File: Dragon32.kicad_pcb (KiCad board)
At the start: 2 copper layers, 253 x 169.1 mm, 139 parts, among them IC10 74ACT138, IC11 74ACT244N, IC16 74ACT244N, IC18 74ACT08, IC19 MC6809E, IC20 MC14529B, IC24 74ACT244N, IC25 LM393P, IC31 74ACT02, IC33 74AACT138N, IC34 CD4050BDR, J1 Video Output Female, J2 Board Interconnect Female, J3 Conn_02x08_Odd_Even, J4 JTAG, J5 6-bit DAC, SW1 RESET, U1 AS6C1008-TIN, U2 AS6C1008-55TIN, U3 XC95144XL-TQ100, U4 TPS7A2433DBVR, U5 W65C21, U6 W65C21, U7 W65C21, U8 28C256, X1 14.31818MHz

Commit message: serial wiring
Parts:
- removed IC18: 74ACT08, Package_SO:SOIC-14_3.9x8.7mm_P1.27mm
- removed IC20: MC14529B, Package_DIP:DIP-16_W7.62mm
- removed IC25: LM393P, Package_DIP:DIP-8_W7.62mm
- added C10: 100n, Capacitor_SMD:C_0805_2012Metric_Pad1.18x1.45mm_HandSolder, F.Cu at (154.9, 79.4)
- added C17: 100n, Capacitor_SMD:C_0805_2012Metric_Pad1.18x1.45mm_HandSolder, F.Cu at (121.1, 77.0)
- added C18: 1u, Capacitor_Tantalum_SMD:CP_EIA-3216-18_Kemet-A_Pad1.58x1.35mm_HandSolder, F.Cu at (137.0, 37.0)
- added C19: 1u, Capacitor_Tantalum_SMD:CP_EIA-3216-18_Kemet-A_Pad1.58x1.35mm_HandSolder, F.Cu at (145.2, 37.0)
- added D10: 1N914, Diode_SMD:D_SOD-323_HandSoldering, F.Cu at (133.3, 74.4)
- added D11: 1N914, Diode_SMD:D_SOD-323_HandSoldering, B.Cu at (133.3, 74.4)
- added D12: 1N914, Diode_SMD:D_SOD-323_HandSoldering, F.Cu at (121.2, 74.4)
- added D13: 1N914, Diode_SMD:D_SOD-323_HandSoldering, B.Cu at (121.2, 74.4)
- added D14: 1N914, Diode_SMD:D_SOD-323_HandSoldering, B.Cu at (123.4, 59.5)
- added D15: 1N914, Diode_SMD:D_SOD-323_HandSoldering, F.Cu at (123.4, 59.5)
- added D16: 1N914, Diode_SMD:D_SOD-323_HandSoldering, F.Cu at (128.4, 59.5)
- added D17: 1N914, Diode_SMD:D_SOD-323_HandSoldering, B.Cu at (128.4, 59.5)
- added IC1: LM393DR, Package_SO:SOP-8_3.9x4.9mm_P1.27mm, F.Cu at (147.2, 151.1)
- added JP3: Serial, Jumper:SolderJumper-3_P1.3mm_Open_Pad1.0x1.5mm, F.Cu at (143.1, 70.2)
- added PL9: Serial, Dragon:DIN-7_DELTRON_671-0701_Horizontal, F.Cu at (86.5, 135.2)
- added R28: 4K7, Resistor_SMD:R_0805_2012Metric_Pad1.20x1.40mm_HandSolder, B.Cu at (96.2, 81.9)
- added R33: 10M, Resistor_SMD:R_0805_2012Metric_Pad1.20x1.40mm_HandSolder, B.Cu at (147.3, 154.1)
- added R34: 1K, Resistor_SMD:R_0805_2012Metric_Pad1.20x1.40mm_HandSolder, B.Cu at (151.9, 147.4)
- added R35: 47R, Resistor_SMD:R_0805_2012Metric_Pad1.20x1.40mm_HandSolder, B.Cu at (92.7, 129.2)
- added R37: 47R, Resistor_SMD:R_0805_2012Metric_Pad1.20x1.40mm_HandSolder, B.Cu at (92.7, 132.5)
- added R44: 4K7, Resistor_SMD:R_0805_2012Metric_Pad1.20x1.40mm_HandSolder, B.Cu at (98.1, 118.2)
- added R57: 47K, Resistor_SMD:R_0805_2012Metric_Pad1.20x1.40mm_HandSolder, B.Cu at (132.8, 77.0)
- added R58: 47K, Resistor_SMD:R_0805_2012Metric_Pad1.20x1.40mm_HandSolder, B.Cu at (126.9, 76.0)
- added R59: 100K, Resistor_SMD:R_0805_2012Metric_Pad1.20x1.40mm_HandSolder, F.Cu at (120.3, 64.3)
- added R60: 100K, Resistor_SMD:R_0805_2012Metric_Pad1.20x1.40mm_HandSolder, F.Cu at (120.3, 62.3)
- added REG1: LM79L05_TO92, Package_TO_SOT_SMD:SOT-89-3_Handsoldering, F.Cu at (141.2, 38.0)
- added U10: 4052, Package_SO:TSSOP-16_4.4x5mm_P0.65mm, F.Cu at (148.5, 133.8)
- added U11: TS5A3166DBVR, Package_TO_SOT_SMD:SOT-23-5, F.Cu at (149.8, 141.1)
- added U12: ~, Package_DIP:DIP-28_W15.24mm, F.Cu at (137.1, 47.4)
- added U13: 4069, Package_SO:SOIC-14_3.9x8.7mm_P1.27mm, F.Cu at (127.1, 66.4)
- added U14: LM348DR, Package_SO:SOIC-14_3.9x8.7mm_P1.27mm, F.Cu at (127.1, 77.0)
- added U9: 74HCT1G08, Package_TO_SOT_SMD:SOT-353_SC-70-5_Handsoldering, B.Cu at (209.3, 116.2)
- added X2: 1.8432MHz, Crystal:Crystal_HC18-U_Horizontal_1EP_style2, F.Cu at (128.0, 54.1)
- C1, C30, C31, C32, C33, C4, C43, C44, D4, D5, D7, D8, D9, R11, R13, R15, R18, R19, R21, R24, R25, R27, R39, R45, R46, R47, R5, R50, R52, R6, R8: moved to F.Cu
- IC10: footprint Package_SO:SOIC-20W_7.5x12.8mm_P1.27mm -> Package_SO:SOIC-16W_7.5x10.3mm_P1.27mm
- IC33: value 74AACT138N -> 74ACT138N; footprint Package_SO:SOIC-20W_7.5x12.8mm_P1.27mm -> Package_SO:SOIC-16W_7.5x10.3mm_P1.27mm
- R31: value 4K7 -> 10K
- R53: value 10M -> 4K7
- R54: value 1K -> 4K7
- R55: value 10K -> 4K7
- TR1: value PN2222 -> PZT2222A; footprint Package_TO_SOT_THT:TO-92_Inline_Wide -> Package_TO_SOT_SMD:SOT-223-3_TabPin2
- moved R38 279.0 mm to (91.3, 175.6)
- moved R29 191.1 mm to (214.8, 156.6), turned to 180 degrees
- moved R16 186.8 mm to (214.8, 152.5)
- moved C26 185.3 mm to (214.8, 154.6)
- moved R56 169.9 mm to (197.0, 191.6), turned to 90 degrees
- moved C11 169.4 mm to (221.7, 46.0), turned to 90 degrees
- moved C12 162.0 mm to (226.7, 52.8), turned to -90 degrees
- moved R63 158.1 mm to (208.5, 182.6), turned to 180 degrees
- moved D6 157.4 mm to (109.3, 37.6), turned to 180 degrees
- moved D5 155.1 mm to (109.3, 41.6), turned to 0 degrees
- moved R36 154.9 mm to (109.3, 35.5)
- moved D4 154.6 mm to (109.4, 39.6), turned to 0 degrees
- moved C13 145.4 mm to (215.0, 53.3), turned to 0 degrees
- moved C48 142.7 mm to (211.5, 155.6), turned to -90 degrees
- moved C14 140.6 mm to (238.4, 64.2), turned to 0 degrees
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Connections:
- IC16 pad 11: DO7 -> DO3
- IC16 pad 12: D6 -> D4
- IC16 pad 13: DO1 -> DO2
- IC16 pad 14: D5 -> D0
- IC16 pad 15: DO0 -> DO5
- IC16 pad 16: D2 -> D1
- IC16 pad 17: DO4 -> DO6
- IC16 pad 18: D3 -> D7
- IC16 pad 2: DO3 -> DO7
- IC16 pad 3: D4 -> D6
- IC16 pad 4: DO2 -> DO1
- IC16 pad 5: D0 -> D5
- IC16 pad 6: DO5 -> DO0
- IC16 pad 7: D1 -> D2
- IC16 pad 8: DO6 -> DO4
- IC16 pad 9: D7 -> D3
- IC34 pad 10: DAC5 -> DAC2
- IC34 pad 11: PIADAC3 -> PIADAC1
- IC34 pad 12: DAC3 -> DAC1
- IC34 pad 2: DAC1 -> DAC5
- IC34 pad 3: PIADAC1 -> PIADAC5
- IC34 pad 4: DAC2 -> DAC4
- IC34 pad 5: PIADAC2 -> PIADAC4
- IC34 pad 6: DAC4 -> DAC3
- IC34 pad 7: PIADAC4 -> PIADAC3
- IC34 pad 9: PIADAC5 -> PIADAC2
- PL6 pad 1: +12V -> BIAS
- PL6 pad 3: -5V -> SOUND
- PL6 pad 4: GND -> VID OUT
- PL6 pad 6: VID OUT -> GND
- PL6 pad 7: SOUND -> -12V
- PL6 pad 9: BIAS -> +12V
- R2 pad 1: unconnected-(R2-Pad1) -> ~{RAS0}
- R31 pad 1: CASS -> Net-(IC1B-+)
- R31 pad 2: +5V -> Net-(U10-X)
- R53 pad 1: PA7 -> Net-(PL9-Pad7)
- R53 pad 2: Net-(IC25B-+) -> -12V
- R54 pad 1: +5V -> Net-(PL9-Pad5)
- R54 pad 2: PA7 -> Net-(D10-A)
- R55 pad 1: Net-(IC25B-+) -> Net-(PL9-Pad2)
- TR1 pad 1: GND -> Net-(TR1-B)
- TR1 pad 2: Net-(TR1-B) -> Net-(D1-A)
- TR1 pad 3: Net-(D1-A) -> GND
- U5 pad 24: +5V -> Net-(JP3-C)
- U5 pad 26: +5V -> Net-(JP3-C)
- U7 pad 11: Alpha -> RC
- U7 pad 12: Inverse -> RClk
- U7 pad 14: RClk -> Inverse
- U7 pad 15: RC -> Alpha
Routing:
- net +5V: track 0.00 -> 1586.9 mm, vias 0 -> 37
- net R/~{W}: track 0.00 -> 592.3 mm, vias 0 -> 15
- net D7: track 0.00 -> 539.6 mm, vias 0 -> 11
- net D6: track 0.00 -> 531.6 mm, vias 0 -> 10
- net D4: track 0.00 -> 529.8 mm, vias 0 -> 11
- net D1: track 0.00 -> 526.3 mm, vias 0 -> 11
- net D0: track 0.00 -> 520.6 mm, vias 0 -> 10
- net D5: track 0.00 -> 520.4 mm, vias 0 -> 10
- net A1: track 0.00 -> 518.5 mm, vias 0 -> 11
- net A0: track 0.00 -> 515.7 mm, vias 0 -> 11
- net ~{RES}: track 0.00 -> 512.4 mm, vias 0 -> 9
- net D2: track 0.00 -> 508.1 mm, vias 0 -> 11
- net D3: track 0.00 -> 508.0 mm, vias 0 -> 10
- net E: track 0.00 -> 490.2 mm, vias 0 -> 11
- net +12V: track 0.00 -> 450.8 mm, vias 0 -> 4
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- added copper zone on B.Cu, net +12V
- added copper zone on B.Cu, net +5V
- added copper zone on F.Cu, net +5V
- added copper zone on F.Cu, net -5V

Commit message: add audio circuits
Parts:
- added C20: 18pF, Capacitor_SMD:C_0805_2012Metric_Pad1.18x1.45mm_HandSolder, F.Cu at (174.6, 25.9)
- added C21: 100nF, Capacitor_SMD:C_0805_2012Metric_Pad1.18x1.45mm_HandSolder, F.Cu at (177.6, 25.9)
- added C24: 18pF, Capacitor_SMD:C_0805_2012Metric_Pad1.18x1.45mm_HandSolder, F.Cu at (180.6, 25.9)
- added C25: 18pF, Capacitor_SMD:C_0805_2012Metric_Pad1.18x1.45mm_HandSolder, F.Cu at (183.6, 25.9)
- added C28: 100nF, Capacitor_SMD:C_0805_2012Metric_Pad1.18x1.45mm_HandSolder, F.Cu at (186.6, 25.9)
- added C29: 18pF, Capacitor_SMD:C_0805_2012Metric_Pad1.18x1.45mm_HandSolder, F.Cu at (174.6, 21.1)
- added C34: 100nF, Capacitor_SMD:C_0805_2012Metric_Pad1.18x1.45mm_HandSolder, F.Cu at (177.6, 21.1)
- added C36: 100nF, Capacitor_SMD:C_0805_2012Metric_Pad1.18x1.45mm_HandSolder, F.Cu at (180.6, 21.1)
- added C37: 2.2nF, Capacitor_SMD:C_0805_2012Metric_Pad1.18x1.45mm_HandSolder, F.Cu at (183.6, 21.1)
- added C40: 2.2nF, Capacitor_SMD:C_0805_2012Metric_Pad1.18x1.45mm_HandSolder, F.Cu at (186.6, 21.1)
- added C41: 2.2nF, Capacitor_SMD:C_0805_2012Metric_Pad1.18x1.45mm_HandSolder, F.Cu at (174.6, 16.3)
- added C46: 10uF, Capacitor_SMD:CP_Elec_5x3, F.Cu at (178.6, 50.4)
- added C47: 2.2nF, Capacitor_SMD:C_0805_2012Metric_Pad1.18x1.45mm_HandSolder, F.Cu at (177.6, 16.3)
- added C49: 2.2nF, Capacitor_SMD:C_0805_2012Metric_Pad1.18x1.45mm_HandSolder, F.Cu at (180.6, 16.3)
- added C50: 2.2nF, Capacitor_SMD:C_0805_2012Metric_Pad1.18x1.45mm_HandSolder, F.Cu at (183.6, 16.3)
- added C51: 10uF, Capacitor_SMD:CP_Elec_5x3, F.Cu at (194.3, 50.3)
- added J6: UART, Connector_PinHeader_1.27mm:PinHeader_1x04_P1.27mm_Vertical, F.Cu at (162.5, 56.3)
- added J7: ICSP, Connector_PinHeader_1.27mm:PinHeader_2x03_P1.27mm_Vertical, F.Cu at (181.3, 56.6)
- added J8: UART, Connector_PinHeader_1.27mm:PinHeader_1x04_P1.27mm_Vertical, F.Cu at (187.3, 55.0)
- added J9: ICSP, Connector_PinHeader_1.27mm:PinHeader_2x03_P1.27mm_Vertical, F.Cu at (203.4, 60.0)
- added JP5: J1 CFG0, Jumper:SolderJumper-2_P1.3mm_Open_Pad1.0x1.5mm, F.Cu at (187.7, 37.3)
- added JP7: J2 CFG1, Jumper:SolderJumper-2_P1.3mm_Open_Pad1.0x1.5mm, F.Cu at (187.7, 40.9)
- added R61: 3.6K, Resistor_SMD:R_0805_2012Metric_Pad1.20x1.40mm_HandSolder, F.Cu at (189.6, 25.9)
- added R62: 3.6K, Resistor_SMD:R_0805_2012Metric_Pad1.20x1.40mm_HandSolder, F.Cu at (192.6, 25.9)
- added R64: 3.6K, Resistor_SMD:R_0805_2012Metric_Pad1.20x1.40mm_HandSolder, F.Cu at (195.5, 25.9)
- added R65: 1K, Resistor_SMD:R_0805_2012Metric_Pad1.20x1.40mm_HandSolder, F.Cu at (198.5, 25.9)
- added R66: 1K, Resistor_SMD:R_0805_2012Metric_Pad1.20x1.40mm_HandSolder, F.Cu at (201.4, 25.9)
- added R67: 1K, Resistor_SMD:R_0805_2012Metric_Pad1.20x1.40mm_HandSolder, F.Cu at (189.6, 21.2)
- added R68: 1K, Resistor_SMD:R_0805_2012Metric_Pad1.20x1.40mm_HandSolder, F.Cu at (192.6, 21.2)
- added R69: 3.6K, Resistor_SMD:R_0805_2012Metric_Pad1.20x1.40mm_HandSolder, F.Cu at (195.5, 21.2)
- added R70: 3.6K, Resistor_SMD:R_0805_2012Metric_Pad1.20x1.40mm_HandSolder, F.Cu at (198.5, 21.2)
- added R71: 3.6K, Resistor_SMD:R_0805_2012Metric_Pad1.20x1.40mm_HandSolder, F.Cu at (201.4, 21.2)
- added R72: 1K, Resistor_SMD:R_0805_2012Metric_Pad1.20x1.40mm_HandSolder, F.Cu at (189.6, 16.4)
- added R73: 1K, Resistor_SMD:R_0805_2012Metric_Pad1.20x1.40mm_HandSolder, F.Cu at (192.6, 16.4)
- added R74: 1K, Resistor_SMD:R_0805_2012Metric_Pad1.20x1.40mm_HandSolder, F.Cu at (195.5, 16.4)
- added R75: 1K, Resistor_SMD:R_0805_2012Metric_Pad1.20x1.40mm_HandSolder, F.Cu at (198.5, 16.4)
- added U15: ATmega48PA-A, Package_QFP:TQFP-32_7x7mm_P0.8mm, F.Cu at (174.0, 68.3)
- added U16: ATmega48PA-A, Package_QFP:TQFP-32_7x7mm_P0.8mm, F.Cu at (195.2, 68.3)
- added U17: 74LS08, Package_SO:SO-14_3.9x8.65mm_P1.27mm, F.Cu at (202.7, 51.9)
- added X3: 27MHz, Crystal:Crystal_SMD_3225-4Pin_3.2x2.5mm_HandSoldering, F.Cu at (171.0, 59.3)
- added X4: 27MHz, Crystal:Crystal_SMD_3225-4Pin_3.2x2.5mm_HandSoldering, F.Cu at (192.3, 59.2)
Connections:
- net SOUND renamed OUT_L
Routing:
- net OUT_L: track 213.2 -> 248.6 mm
- net VCLK: track 284.2 -> 298.1 mm, vias 5 -> 3
- net A2: track 420.2 -> 416.0 mm, vias 10 -> 9
- net GND: vias 120 -> 121

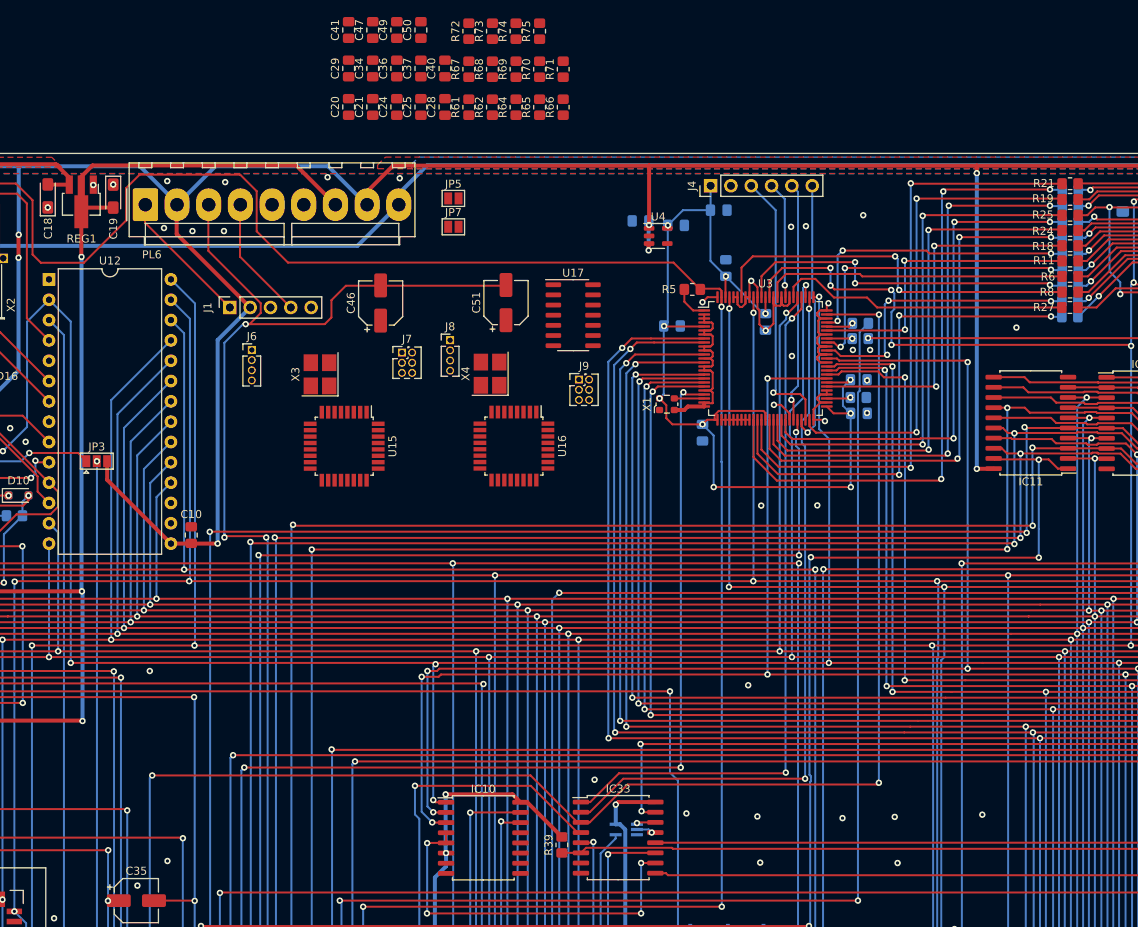
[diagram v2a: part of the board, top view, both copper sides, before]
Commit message: complete audio routing
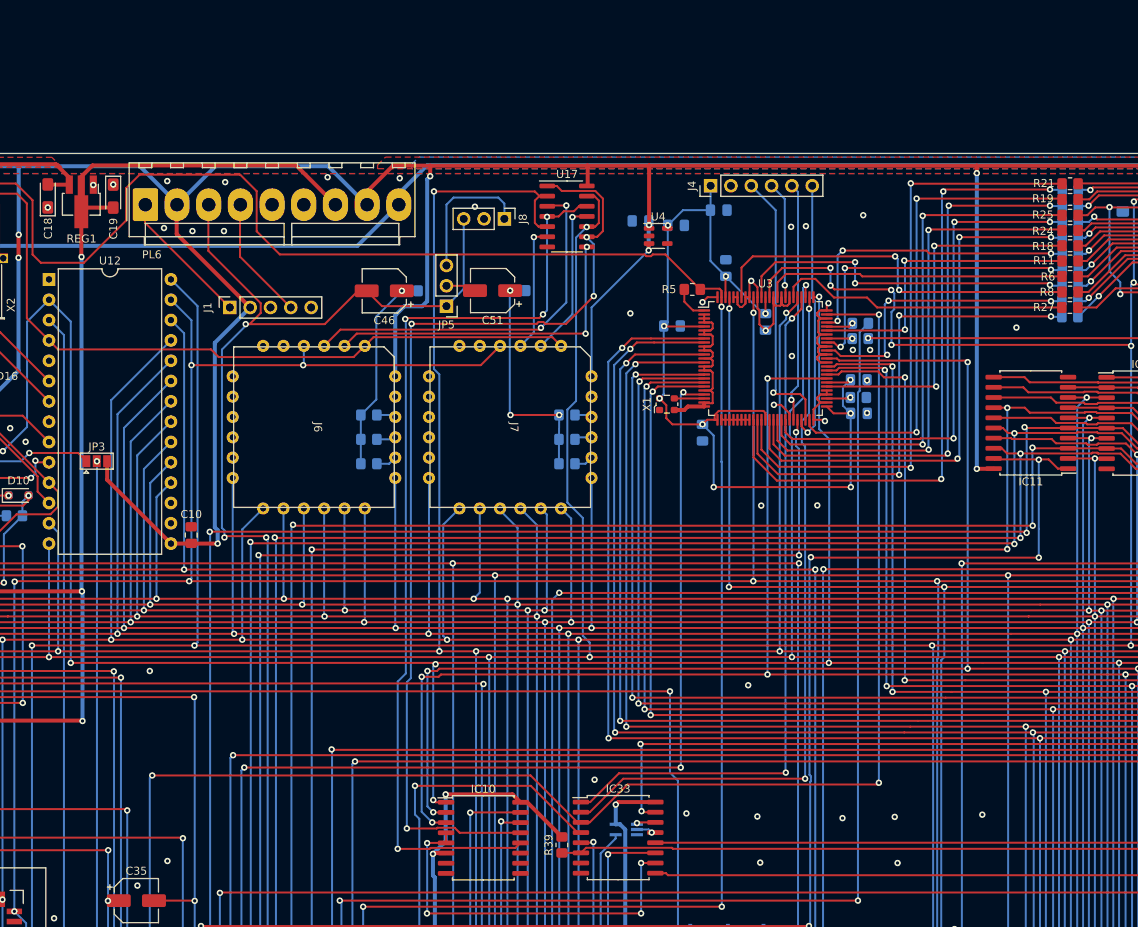
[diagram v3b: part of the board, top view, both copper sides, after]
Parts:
- removed C20, C24, C25, C29: 18pF, Capacitor_SMD:C_0805_2012Metric_Pad1.18x1.45mm_HandSolder
- removed C21, C28, C34, C36: 100nF, Capacitor_SMD:C_0805_2012Metric_Pad1.18x1.45mm_HandSolder
- removed C37, C40, C41, C47, C49, C50: 2.2nF, Capacitor_SMD:C_0805_2012Metric_Pad1.18x1.45mm_HandSolder
- removed J9: ICSP, Connector_PinHeader_1.27mm:PinHeader_2x03_P1.27mm_Vertical
- removed JP7: J2 CFG1, Jumper:SolderJumper-2_P1.3mm_Open_Pad1.0x1.5mm
- removed R61, R62, R64, R69, R70, R71: 3.6K, Resistor_SMD:R_0805_2012Metric_Pad1.20x1.40mm_HandSolder
- removed U15, U16: ATmega48PA-A, Package_QFP:TQFP-32_7x7mm_P0.8mm
- removed X3, X4: 27MHz, Crystal:Crystal_SMD_3225-4Pin_3.2x2.5mm_HandSoldering
- J6: value UART -> Audio Left; footprint Connector_PinHeader_1.27mm:PinHeader_1x04_P1.27mm_Vertical -> Dragon:AY-QTHT
- J7: value ICSP -> Audio Right; footprint Connector_PinHeader_1.27mm:PinHeader_2x03_P1.27mm_Vertical -> Dragon:AY-QTHT
- J8: value UART -> Stereo; footprint Connector_PinHeader_1.27mm:PinHeader_1x04_P1.27mm_Vertical -> Connector_PinHeader_2.54mm:PinHeader_1x03_P2.54mm_Vertical
- JP5: value J1 CFG0 -> Jumper_3_Open; footprint Jumper:SolderJumper-2_P1.3mm_Open_Pad1.0x1.5mm -> Connector_PinHeader_2.54mm:PinHeader_1x03_P2.54mm_Vertical
- R65, R66, R67, R68, R72, R73, R74, R75: moved to B.Cu
- U12: value ~ -> 6551
- moved R74 54.4 mm to (201.9, 70.5), turned to 180 degrees
- moved R73 51.9 mm to (201.9, 67.4), turned to 180 degrees
- moved R67 50.9 mm to (177.1, 70.5), turned to 180 degrees
- moved R72 49.5 mm to (201.9, 64.4), turned to 180 degrees
- moved R66 48.1 mm to (177.1, 67.4), turned to 180 degrees
- moved R65 44.0 mm to (177.1, 64.4), turned to 180 degrees
- moved R75 32.5 mm to (195.7, 48.8), turned to 180 degrees
- moved R68 29.6 mm to (182.3, 48.9), turned to 180 degrees
- moved J8 16.6 mm to (194.1, 39.9), turned to -90 degrees
- moved J7 16.4 mm to (194.8, 65.9), turned to -90 degrees
- moved JP5 13.5 mm to (186.8, 50.8), turned to 180 degrees
- moved J6 12.4 mm to (170.3, 65.9), turned to -90 degrees
- moved U17 12.4 mm to (201.9, 39.6)
- moved C51 2.25 mm to (192.6, 48.8), turned to 180 degrees
- moved C46 1.59 mm to (179.0, 48.9), turned to 180 degrees
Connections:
- C51 pad 2: OUT_L -> OUT_R
- J6 pad 1: GND -> +5V
- J6 pad 2: +5V -> GND
- J6 pad 3: TX1 -> OUT_A
- J6 pad 4: RX1 -> OUT_B
- J7 pad 2: MISO1 -> GND
- J7 pad 3: MOSI1 -> OUT_D
- J7 pad 4: SCK -> OUT_E
- J7 pad 5: GND -> OUT_F
- J7 pad 6: ~{RES} -> D5
- J8 pad 1: GND -> Net-(J8-Pin_1)
- J8 pad 2: +5V -> GND
- J8 pad 3: TX1 -> OUT_L
- JP5 pad 1: GND -> OUT_L
- JP5 pad 2: CFG_0 -> OUT_R
- U17 pad 1: SEL -> P1c
- U17 pad 10: ~{R}/W -> A1
- U17 pad 11: unconnected-(U17-Pad11) -> BC11
- U17 pad 12: SEL -> P1d
- U17 pad 13: A2 -> A1
- U17 pad 3: BDIR -> BDIR0
- U17 pad 4: SEL -> P1d
- U17 pad 5: A1 -> A0
- U17 pad 6: unconnected-(U17-Pad6) -> BDIR1
- U17 pad 8: BC1 -> BC10
- U17 pad 9: SEL -> P1c
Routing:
- net P1c: track 0.00 -> 124.0 mm, vias 0 -> 4
- net P1d: track 0.00 -> 117.8 mm, vias 0 -> 4
- net A0: track 515.7 -> 594.2 mm, vias 11 -> 13
- net ~{RES}: track 512.4 -> 578.7 mm
- net A1: track 518.5 -> 580.7 mm, vias 11 -> 13
- net +5V: track 1587.0 -> 1639.9 mm, vias 37 -> 38
- net BDIR0: track 0.00 -> 47.1 mm, vias 0 -> 2
- net E: track 490.2 -> 532.4 mm, vias 11 -> 13
- net BC10: track 0.00 -> 41.7 mm, vias 0 -> 2
- net D6: track 531.6 -> 570.7 mm, vias 10 -> 12
- net D5: track 520.4 -> 558.0 mm, vias 10 -> 12
- net D7: track 539.6 -> 574.5 mm, vias 11 -> 13
- net D4: track 529.8 -> 558.8 mm, vias 11 -> 13
- net Net-(C51-Pad1): track 0.00 -> 27.9 mm, vias 0 -> 3
- net D3: track 508.0 -> 535.8 mm, vias 10 -> 11
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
